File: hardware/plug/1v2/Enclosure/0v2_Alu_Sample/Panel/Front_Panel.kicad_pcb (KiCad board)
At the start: 2 copper layers, 65.8 x 46.2 mm, 25 parts

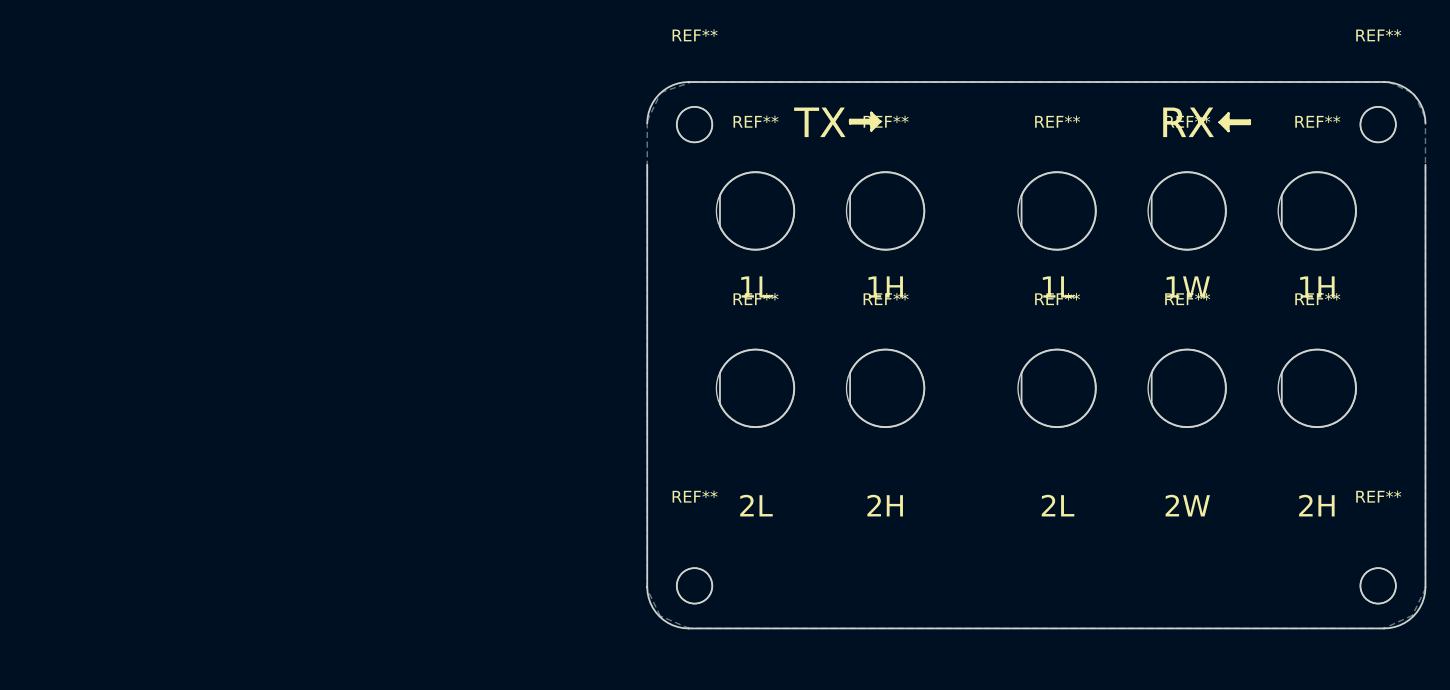
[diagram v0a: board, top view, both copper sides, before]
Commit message: Update on 0v2, enclosure 97x40x100
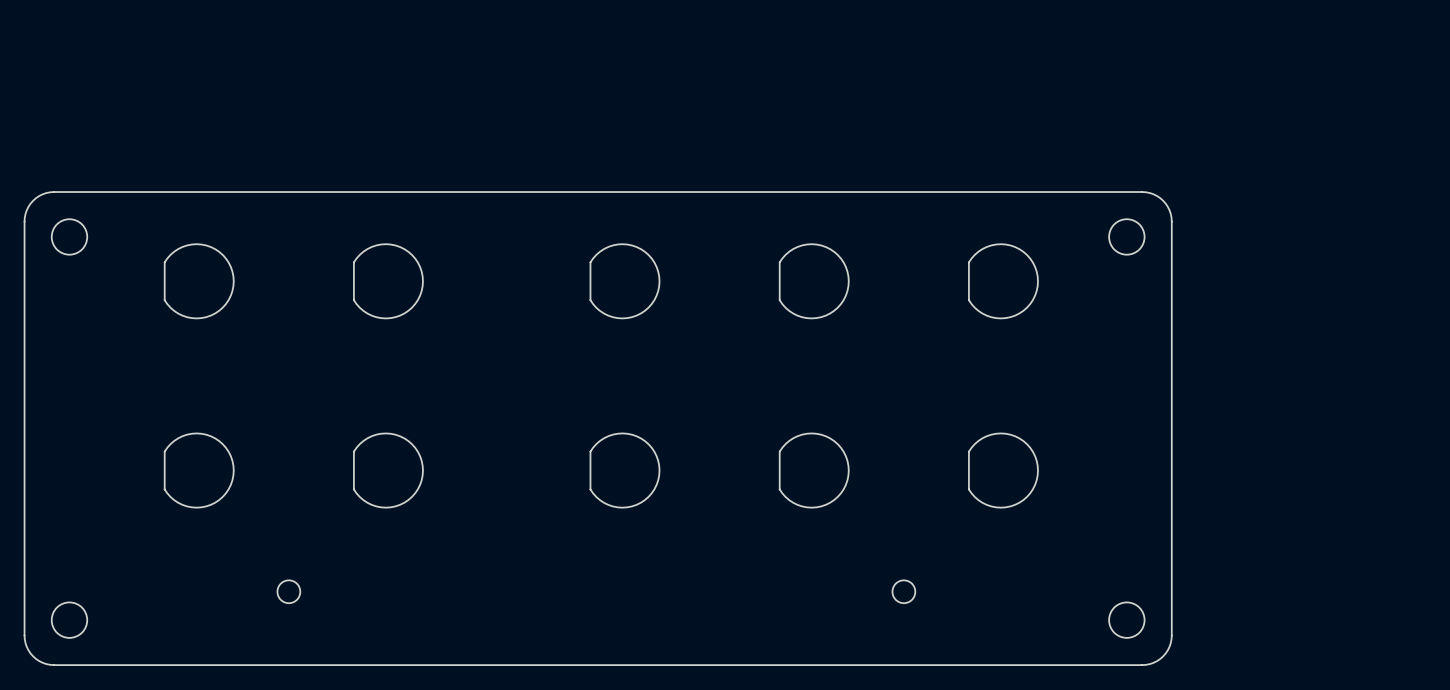
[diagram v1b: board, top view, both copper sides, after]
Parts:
- removed the REF** at (162.8, 38.9)
- removed the REF** at (135.6, 46.2) (x2)
- removed the REF** at (121.1, 61.2) (x2)
- removed the REF** at (110.1, 61.2) (x2)
- removed the REF** at (121.1, 46.2) (x2)
- removed the REF** at (101.0, 81.5)
- removed the REF** at (157.6, 46.2) (x2)
- removed the REF** at (135.6, 61.2) (x2)
- removed the REF** at (146.6, 61.2) (x2)
- removed the REF** at (157.6, 61.2) (x2)
- removed the REF** at (105.0, 38.9)
- removed the REF** at (146.6, 46.2) (x2)
- removed the REF** at (110.1, 46.2) (x2)
- removed the REF** at (105.0, 77.9)
- removed the REF** at (162.8, 77.9)
- added REF**: 2, Ohisja:SMA_front_panel_12.5_antenna, F.Cu at (130.8, 68.2)
- added REF**: 2, Ohisja:SMA_front_panel_12.5_antenna, F.Cu at (62.9, 52.1)
- added REF**: 2, Ohisja:SMA_front_panel_12.5_antenna, F.Cu at (114.8, 68.2)
- added REF**: 2, Ohisja:SMA_front_panel_12.5_antenna, F.Cu at (98.8, 68.2)
- added REF**: 2, Ohisja:SMA_front_panel_12.5_antenna, F.Cu at (78.8, 68.2)
- added REF**: 2, Ohisja:SMA_front_panel_12.5_antenna, F.Cu at (62.9, 68.2)
- added REF**: 2, Ohisja:SMA_front_panel_12.5_antenna, F.Cu at (130.8, 52.1)
- added REF**: 2, Ohisja:SMA_front_panel_12.5_antenna, F.Cu at (114.8, 52.1)
- added REF**: 2, Ohisja:SMA_front_panel_12.5_antenna, F.Cu at (98.8, 52.1)
- added REF**: 2, Ohisja:SMA_front_panel_12.5_antenna, F.Cu at (78.8, 52.1)
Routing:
- removed copper zone on B.Cu, net (none)
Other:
- board size 65.8 x 46.2 mm -> 97 x 40 mm
- board text removed: "1H"
- board text removed: "1L"
- board text removed: "1W"
- board text removed: "2H"
- board text removed: "2L"
- board text removed: "2W"
- board text removed: "RX"
- board text removed: "TX"
